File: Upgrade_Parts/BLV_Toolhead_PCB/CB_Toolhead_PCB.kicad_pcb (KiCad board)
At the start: 2 copper layers, 14 parts, among them J1 Micro-Fit, J10 RB1-125B8G1A, J2 JST-4, J3 JST-2, J4 JST-2, J5 JST-2, J6 JST-2, J8 JST-3, J9 JST-2, U1 SN65LVDS2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

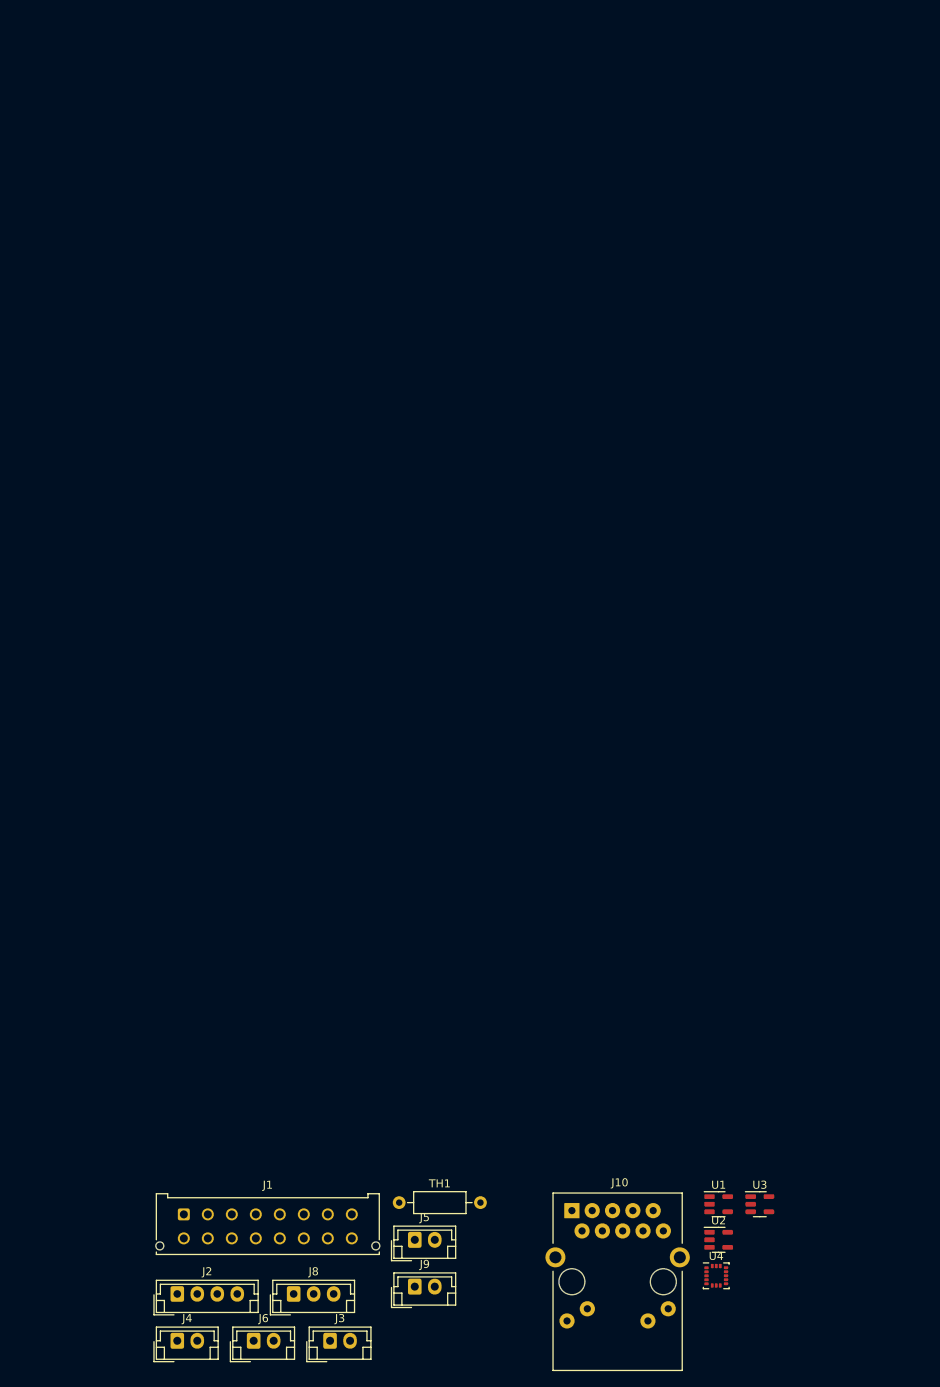
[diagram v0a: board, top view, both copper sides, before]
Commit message: replaced lvds drver
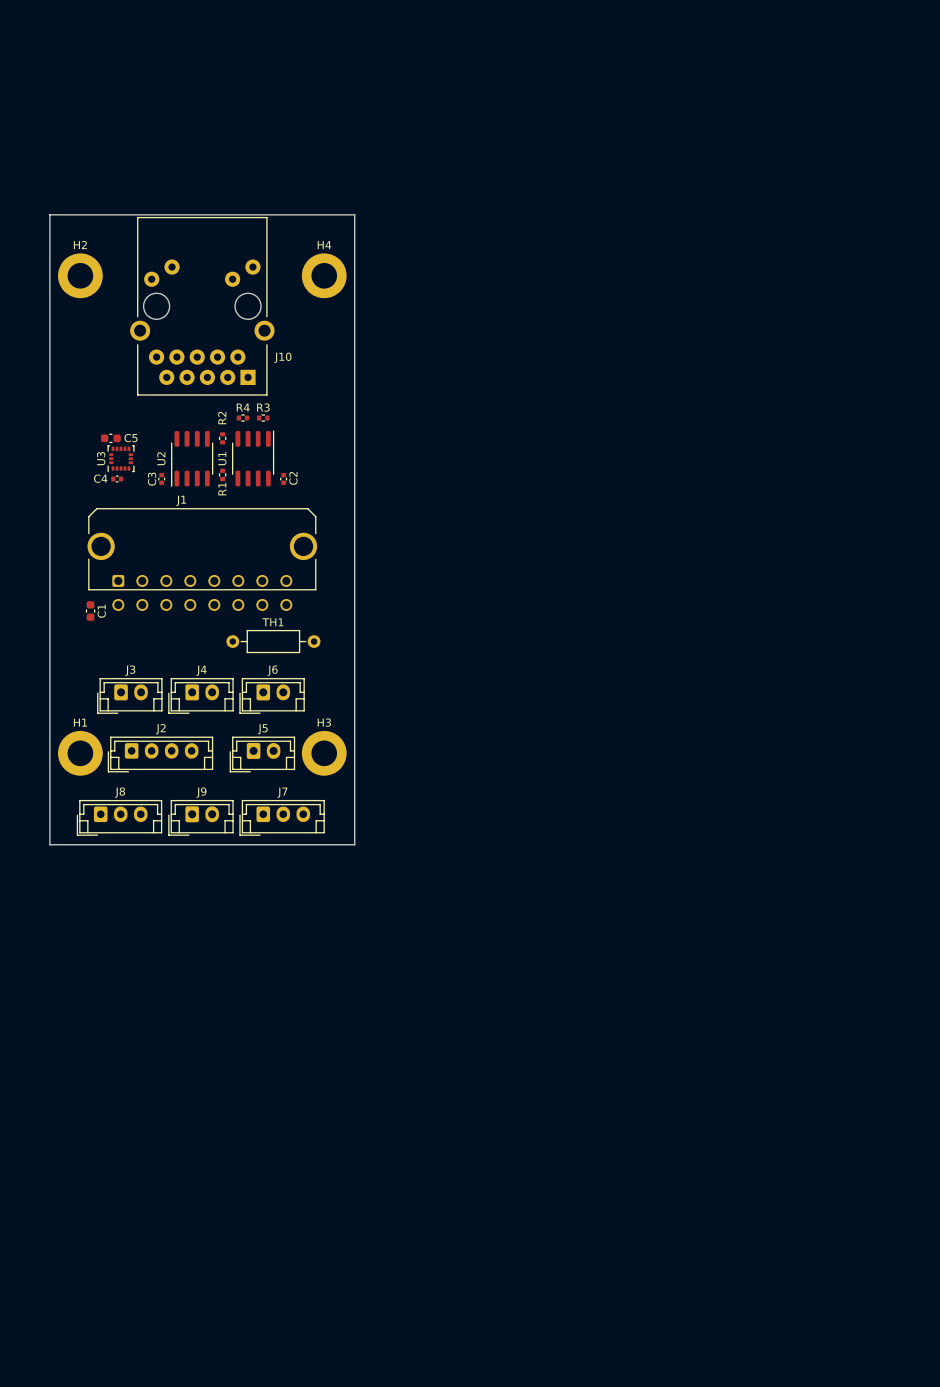
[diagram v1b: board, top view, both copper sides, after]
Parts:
- removed U4: LIS3DH, Package_LGA:LGA-16_3x3mm_P0.5mm_LayoutBorder3x5y
- added C1: 10u, Capacitor_SMD:C_0603_1608Metric, F.Cu at (62.2, 88.9)
- added C2: 100n, Capacitor_SMD:C_0402_1005Metric, F.Cu at (86.4, 72.4)
- added C3: 100n, Capacitor_SMD:C_0402_1005Metric, F.Cu at (71.1, 72.4)
- added C4: 100n, Capacitor_SMD:C_0402_1005Metric, F.Cu at (65.6, 72.4)
- added C5: 10u, Capacitor_SMD:C_0603_1608Metric, F.Cu at (64.8, 67.3)
- added H1: M3_Mount, MountingHole:MountingHole_3.2mm_M3_DIN965_Pad, F.Cu at (61.0, 106.7)
- added H2: M3_Mount, MountingHole:MountingHole_3.2mm_M3_DIN965_Pad, F.Cu at (61.0, 47.0)
- added H3: M3_Mount, MountingHole:MountingHole_3.2mm_M3_DIN965_Pad, F.Cu at (91.4, 106.7)
- added H4: M3_Mount, MountingHole:MountingHole_3.2mm_M3_DIN965_Pad, F.Cu at (91.4, 47.0)
- added J7: Endstop, Connector_JST:JST_EH_B3B-EH-A_1x03_P2.50mm_Vertical, F.Cu at (83.8, 114.3)
- added R1: 2.1k, Resistor_SMD:R_0402_1005Metric, F.Cu at (78.7, 71.9)
- added R2: 1.2k, Resistor_SMD:R_0402_1005Metric, F.Cu at (78.7, 67.3)
- added R3: 100, Resistor_SMD:R_0402_1005Metric, F.Cu at (83.8, 64.8)
- added R4: 100, Resistor_SMD:R_0402_1005Metric, F.Cu at (81.3, 64.8)
- J1: footprint Connector_Molex:Molex_Micro-Fit_3.0_43045-1612_2x08_P3.00mm_Vertical -> Connector_Molex:Molex_Micro-Fit_3.0_43045-1621_2x08-1MP_P3.00mm_Horizontal
- U1: value SN65LVDS2 -> DS90LV028AQ; footprint Package_TO_SOT_SMD:SOT-23-5 -> Package_SO:SOIC-8_3.9x4.9mm_P1.27mm
- U2: value SN65LVDS1 -> DS90LV027A; footprint Package_TO_SOT_SMD:SOT-23-5 -> Package_SO:SOIC-8_3.9x4.9mm_P1.27mm
- U3: value SN65LVDS1 -> LIS3DH; footprint Package_TO_SOT_SMD:SOT-23-5 -> Package_LGA:LGA-16_3x3mm_P0.5mm_LayoutBorder3x5y
- moved U3 122.7 mm to (66.0, 69.8), turned to 90 degrees
- moved U2 117.7 mm to (74.9, 69.8), turned to 90 degrees
- moved J10 111.7 mm to (81.9, 59.7), turned to 180 degrees
- moved U1 109.9 mm to (82.5, 69.8), turned to -90 degrees
- moved J3 85.2 mm to (66.0, 99.1)
- moved J4 81.1 mm to (74.9, 99.1)
- moved J6 81.1 mm to (83.8, 99.1)
- moved J1 79.6 mm to (65.7, 85.1)
- moved TH1 73.2 mm to (80.0, 92.7)
- moved J2 68.1 mm to (67.4, 106.4)
- moved J9 65.3 mm to (74.9, 114.3)
- moved J8 64.6 mm to (63.5, 114.3)
- moved J5 64.3 mm to (82.6, 106.4)
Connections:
- U1 pad 1: +3V3 -> /Accelerometer/SPI_MOSI_N
- U1 pad 2: GND -> /Accelerometer/SPI_MOSI_P
- U1 pad 3: /Accelerometer/SPI_MOSI_P -> Net-(R4-Pad1)
- U1 pad 4: /Accelerometer/SPI_MOSI_N -> Net-(R4-Pad2)
- U1 pad 5: /Accelerometer/SPI_MISO -> GND
- U2 pad 2: GND -> /Accelerometer/SPI_MOSI
- U2 pad 3: /Accelerometer/SPI_MISO_N -> /Accelerometer/INT1
- U2 pad 4: /Accelerometer/SPI_MISO_P -> GND
- U2 pad 5: /Accelerometer/SPI_MOSI -> /Accelerometer/INT1_N
- U3 pad 2: GND -> unconnected-(U3-Pad2)
- U3 pad 3: /Accelerometer/INT1_N -> unconnected-(U3-Pad3)
- U3 pad 4: /Accelerometer/INT1_P -> /Accelerometer/SPI_SCK
- U3 pad 5: /Accelerometer/INT1 -> GND
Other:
- board outline added: 38.1 x 78.7 mm

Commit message: removed lvds drivers
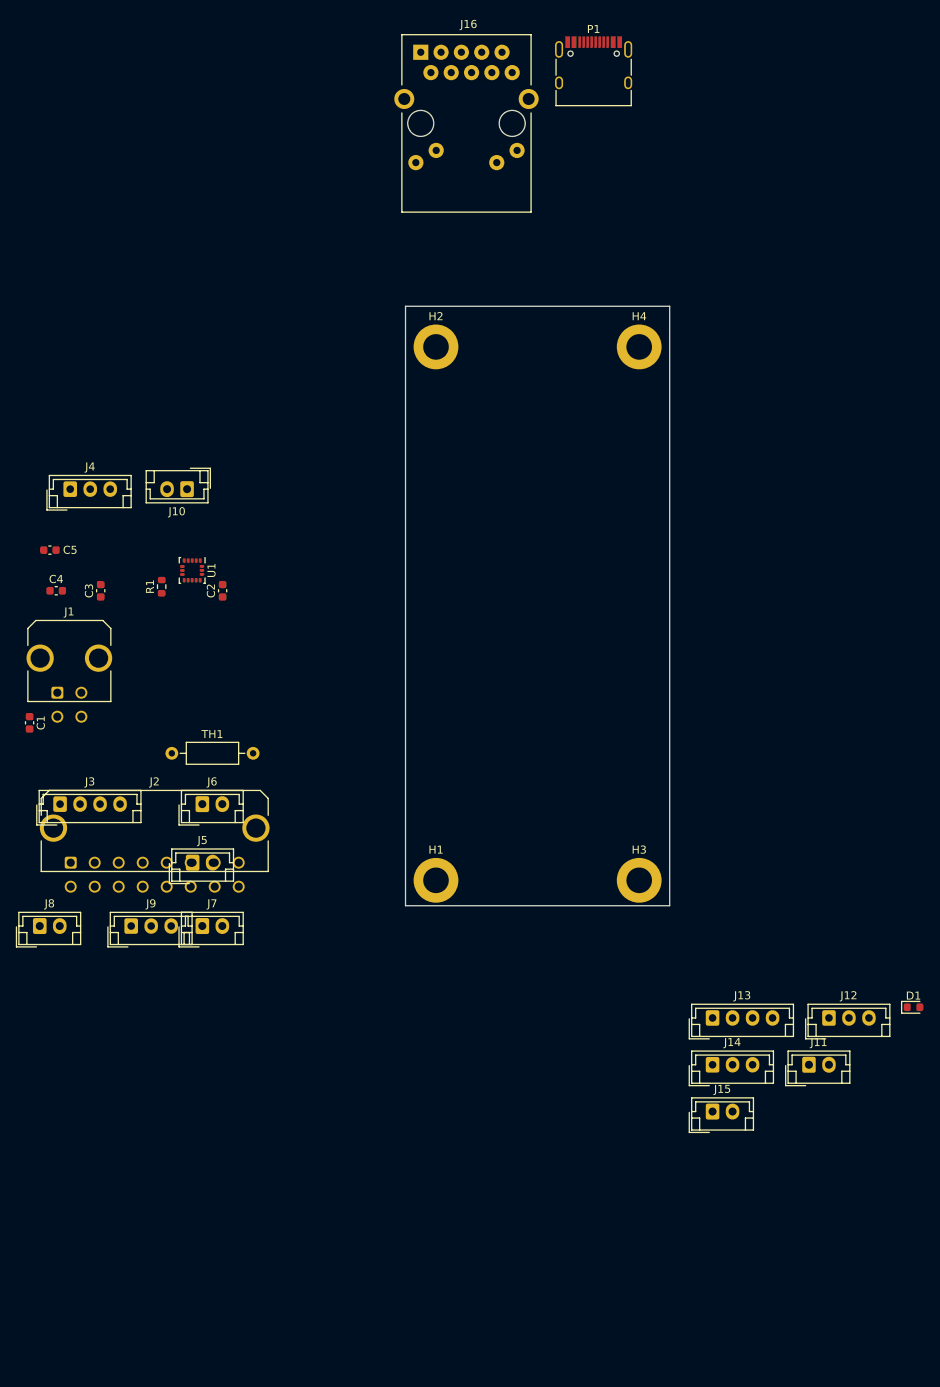
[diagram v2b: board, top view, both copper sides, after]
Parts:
- removed R2: 1.2k, Resistor_SMD:R_0402_1005Metric
- removed R3, R4: 100, Resistor_SMD:R_0402_1005Metric
- removed U2: DS90LV027A, Package_SO:SOIC-8_3.9x4.9mm_P1.27mm
- removed U3: LIS3DH, Package_LGA:LGA-16_3x3mm_P0.5mm_LayoutBorder3x5y
- added D1: BAS, Diode_SMD:D_0603_1608Metric, F.Cu at (165.1, 138.4)
- added J11: JST-2, Connector_JST:JST_EH_B2B-EH-A_1x02_P2.50mm_Vertical, F.Cu at (152.0, 145.6)
- added J12: JST-3, Connector_JST:JST_EH_B3B-EH-A_1x03_P2.50mm_Vertical, F.Cu at (154.5, 139.8)
- added J13: JST-4, Connector_JST:JST_EH_B4B-EH-A_1x04_P2.50mm_Vertical, F.Cu at (140.0, 139.8)
- added J14: JST-3, Connector_JST:JST_EH_B3B-EH-A_1x03_P2.50mm_Vertical, F.Cu at (140.0, 145.6)
- added J15: JST-2, Connector_JST:JST_EH_B2B-EH-A_1x02_P2.50mm_Vertical, F.Cu at (140.0, 151.5)
- added J16: RB1-125B8G1A, Connector_RJ:RJ45_UDE_RB1-125B8G1A, F.Cu at (103.5, 19.1)
- added P1: USB_C_Plug_USB2.0, Connector_USB:USB_C_Receptacle_HRO_TYPE-C-31-M-12, F.Cu at (125.1, 21.8)
- C2, C3: value 100n -> 10u; footprint Capacitor_SMD:C_0402_1005Metric -> Capacitor_SMD:C_0603_1608Metric
- C4: footprint Capacitor_SMD:C_0402_1005Metric -> Capacitor_SMD:C_0603_1608Metric
- J1: value Micro-Fit -> Power; footprint Connector_Molex:Molex_Micro-Fit_3.0_43045-1621_2x08-1MP_P3.00mm_Horizontal -> Connector_Molex:Molex_Micro-Fit_3.0_43045-0421_2x02-1MP_P3.00mm_Horizontal
- J10: value RB1-125B8G1A -> JST-2; footprint Connector_RJ:RJ45_UDE_RB1-125B8G1A -> Connector_JST:JST_EH_B2B-EH-A_1x02_P2.50mm_Vertical
- J2: value JST-4 -> Micro-Fit; footprint Connector_JST:JST_EH_B4B-EH-A_1x04_P2.50mm_Vertical -> Connector_Molex:Molex_Micro-Fit_3.0_43045-1621_2x08-1MP_P3.00mm_Horizontal
- J3: value JST-2 -> JST-4; footprint Connector_JST:JST_EH_B2B-EH-A_1x02_P2.50mm_Vertical -> Connector_JST:JST_EH_B4B-EH-A_1x04_P2.50mm_Vertical
- J4: value JST-2 -> JST-3; footprint Connector_JST:JST_EH_B2B-EH-A_1x02_P2.50mm_Vertical -> Connector_JST:JST_EH_B3B-EH-A_1x03_P2.50mm_Vertical
- J7: value Endstop -> JST-2; footprint Connector_JST:JST_EH_B3B-EH-A_1x03_P2.50mm_Vertical -> Connector_JST:JST_EH_B2B-EH-A_1x02_P2.50mm_Vertical
- J8: value JST-3 -> JST-2; footprint Connector_JST:JST_EH_B3B-EH-A_1x03_P2.50mm_Vertical -> Connector_JST:JST_EH_B2B-EH-A_1x02_P2.50mm_Vertical
- J9: value JST-2 -> Endstop; footprint Connector_JST:JST_EH_B2B-EH-A_1x02_P2.50mm_Vertical -> Connector_JST:JST_EH_B3B-EH-A_1x03_P2.50mm_Vertical
- R1: value 2.1k -> 470R; footprint Resistor_SMD:R_0402_1005Metric -> Resistor_SMD:R_0603_1608Metric
- U1: value DS90LV028AQ -> LIS3DH; footprint Package_SO:SOIC-8_3.9x4.9mm_P1.27mm -> Package_LGA:LGA-16_3x3mm_P0.5mm_LayoutBorder3x5y
- moved H1 47.2 mm to (105.4, 122.6)
- moved H2 45.3 mm to (105.4, 55.9)
- moved H3 42.5 mm to (130.8, 122.6)
- moved H4 40.4 mm to (130.8, 55.9)
- moved J4 29.6 mm to (59.7, 73.7)
- moved J9 15.9 mm to (67.3, 128.3)
- moved TH1 15.9 mm to (72.4, 106.7)
- moved J8 15.9 mm to (55.9, 128.3)
- moved J7 15.9 mm to (76.2, 128.3)
- moved C2 15.9 mm to (78.7, 86.4)
- moved C3 15.9 mm to (63.5, 86.4)
- moved C4 15.9 mm to (57.9, 86.4)
- moved J1 15.9 mm to (58.1, 99.1)
- moved J10 15.9 mm to (74.3, 73.7)
- moved J2 15.9 mm to (59.8, 120.3)
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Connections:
- C1 pad 1: +3V3 -> +24V
- C3 pad 1: +3V3 -> +5V
- J1 pad 3: /x_endstop -> +5V
- J1 pad 4: /heater -> GNDA
- J2 pad 1: Net-(J1-Pad6) -> /x_endstop
- J2 pad 2: Net-(J1-Pad8) -> /heater
- J2 pad 3: Net-(J1-Pad10) -> /z_probe
- J2 pad 4: Net-(J1-Pad12) -> /1A
- J3 pad 1: +24V -> /1A
- J3 pad 2: /toolfan -> /1B
- J4 pad 1: +24V -> +5V
- J4 pad 2: /partfan -> Net-(J4-Pad2)
- J5 pad 2: /heater -> /partfan
- J6 pad 2: /led -> /toolfan
- J7 pad 1: /x_endstop -> +24V
- J7 pad 2: unconnected-(J7-Pad2) -> /heater
- J8 pad 1: +3V3 -> +24V
- J8 pad 2: /z_probe -> /neopixel_do
- J9 pad 1: /thermistor -> /x_endstop
- J9 pad 2: GNDA -> unconnected-(J9-Pad2)
- R1 pad 1: +3V3 -> /neopixel_do
- R1 pad 2: Net-(J10-PadR1) -> Net-(J4-Pad2)
- TH1 pad 1: Net-(J1-Pad14) -> Net-(J2-Pad12)
- U1 pad 1: /Accelerometer/SPI_MOSI_N -> +3V3
- U1 pad 2: /Accelerometer/SPI_MOSI_P -> unconnected-(U1-Pad2)
- U1 pad 3: Net-(R4-Pad1) -> unconnected-(U1-Pad3)
- U1 pad 4: Net-(R4-Pad2) -> /Accelerometer1/SPI_SCK
- U1 pad 6: unconnected-(U1-Pad6) -> /Accelerometer1/SPI_MOSI
- U1 pad 7: /Accelerometer/SPI_MISO -> /Accelerometer1/SPI_MISO
- U1 pad 8: +3V3 -> /Accelerometer1/SPI_CS
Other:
- board size 38.1 x 78.7 mm -> 33 x 74.9 mm
